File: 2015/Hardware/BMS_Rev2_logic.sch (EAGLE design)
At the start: 34 parts, among them Q9 MOSFET-NCHANNEL2N7002PW

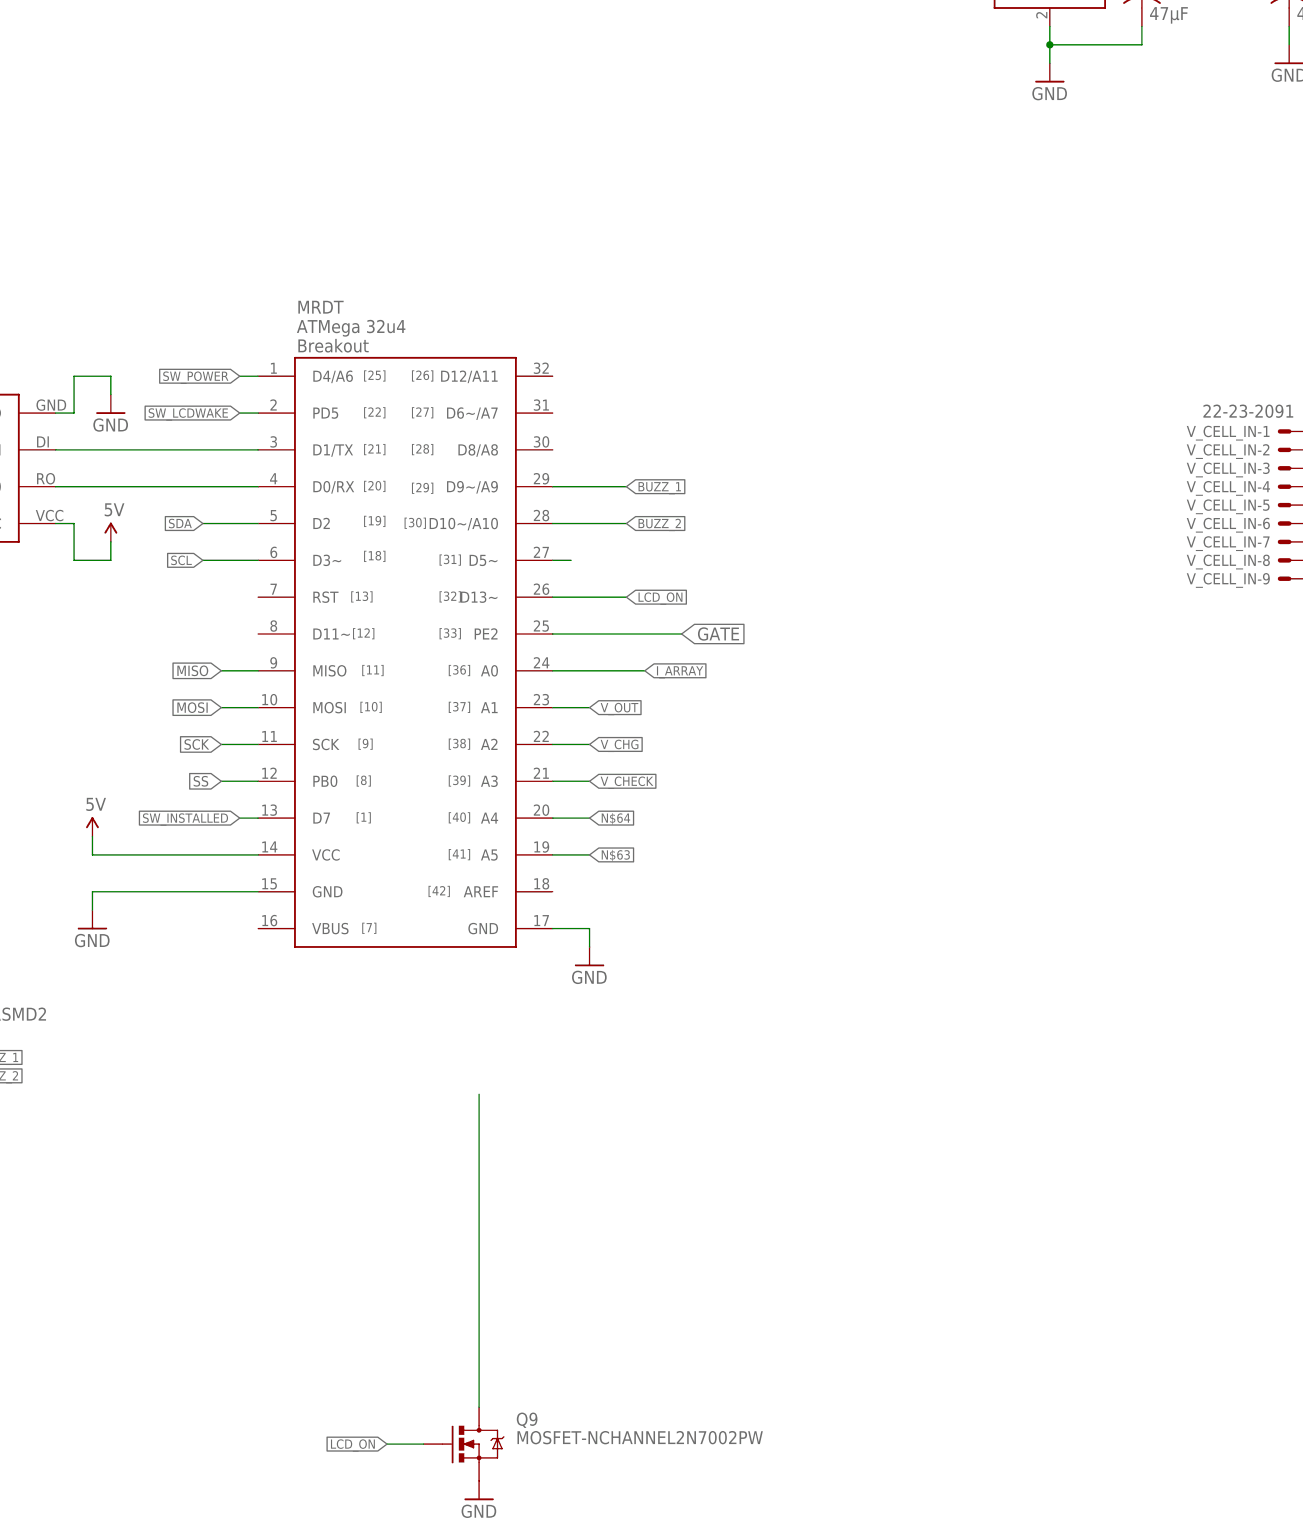
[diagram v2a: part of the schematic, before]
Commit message: Added connection for LCD
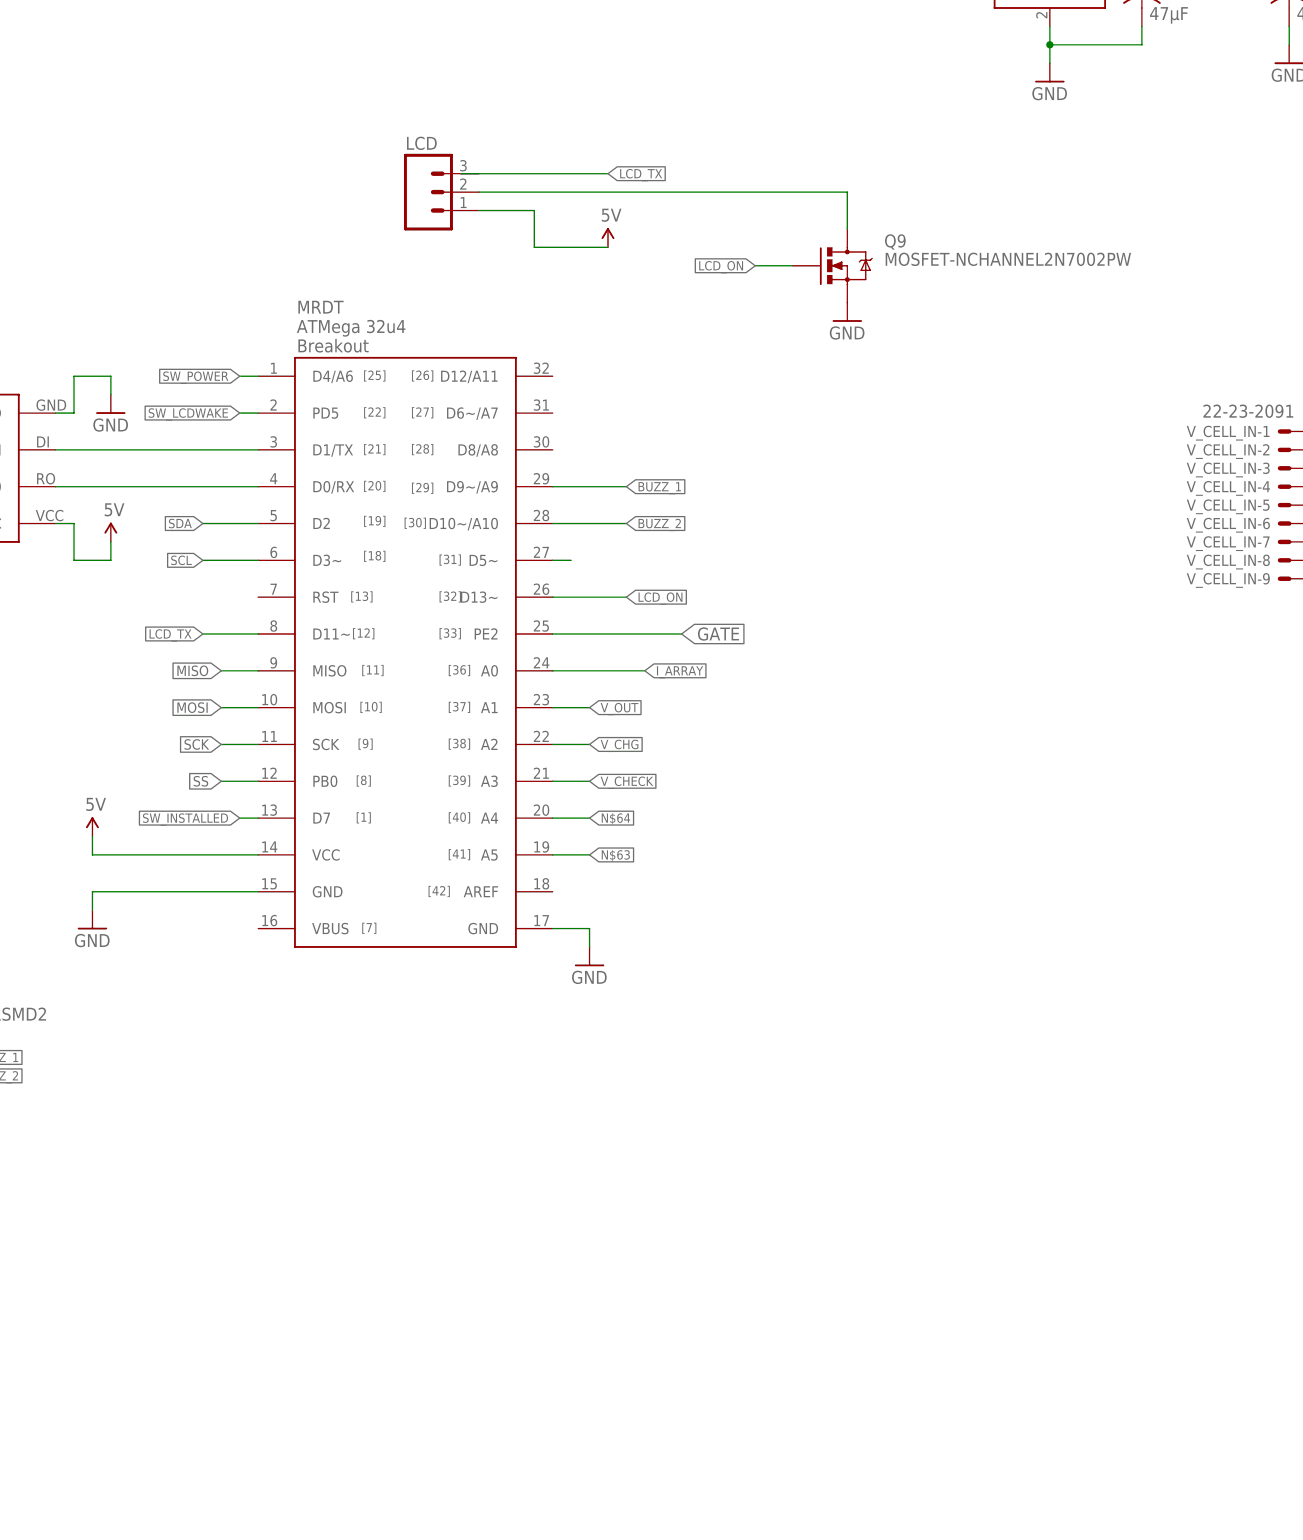
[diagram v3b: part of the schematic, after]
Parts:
- added LCD: (no value), SparkFun-Connectors:M03POLAR
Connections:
- removed net N$32: Q9.D
- new net LCD_TX: U$3.D11~
- new net N$5: LCD.2, Q9.D
- net 5V: now also LCD.1
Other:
- moved on the sheet: Q9
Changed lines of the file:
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@@
 <?xml version="1.0" encoding="utf-8"?>
 <!DOCTYPE eagle SYSTEM "eagle.dtd">
-<eagle version="7.0.0">
+<eagle version="6.5.0">
 <drawing>
 <settings>
@@
 <layers>
 <layer number="1" name="Top" color="4" fill="1" visible="no" active="no"/>
+<layer number="2" name="Route2" color="1" fill="3" visible="no" active="no"/>
+<layer number="3" name="Route3" color="4" fill="3" visible="no" active="no"/>
+<layer number="4" name="Route4" color="1" fill="4" visible="no" active="no"/>
+<layer number="5" name="Route5" color="4" fill="4" visible="no" active="no"/>
+<layer number="6" name="Route6" color="1" fill="8" visible="no" active="no"/>
+<layer number="7" name="Route7" color="4" fill="8" visible="no" active="no"/>
+<layer number="8" name="Route8" color="1" fill="2" visible="no" active="no"/>
+<layer number="9" name="Route9" color="4" fill="2" visible="no" active="no"/>
+<layer number="10" name="Route10" color="1" fill="7" visible="no" active="no"/>
+<layer number="11" name="Route11" color="4" fill="7" visible="no" active="no"/>
+<layer number="12" name="Route12" color="1" fill="5" visible="no" active="no"/>
+<layer number="13" name="Route13" color="4" fill="5" visible="no" active="no"/>
+<layer number="14" name="Route14" color="1" fill="6" visible="no" active="no"/>
+<layer number="15" name="Route15" color="4" fill="6" visible="no" active="no"/>
 <layer number="16" name="Bottom" color="1" fill="1" visible="no" active="no"/>
 <layer number="17" name="Pads" color="2" fill="1" visible="no" active="no"/>
@@
 <part name="GND2" library="SparkFun-Aesthetics" deviceset="GND" device=""/>
 <part name="F9" library="SparkFun-PowerIC" deviceset="PTC" device="SMD"/>
+<part name="LCD" library="SparkFun-Connectors" deviceset="M03" device="POLAR"/>
+<part name="SUPPLY3" library="SparkFun-Aesthetics" deviceset="5V" device=""/>
 </parts>
 <sheets>
@@
 <instance part="V_CELL_IN" gate="-8" x="88.9" y="-35.56" rot="R180"/>
 <instance part="V_CELL_IN" gate="-9" x="88.9" y="-38.1" rot="R180"/>
-<instance part="Q9" gate="G$1" x="-22.86" y="-157.48"/>
-<instance part="GND11" gate="1" x="-22.86" y="-165.1"/>
+<instance part="Q9" gate="G$1" x="27.94" y="5.08"/>
+<instance part="GND11" gate="1" x="27.94" y="-2.54"/>
 <instance part="JP3" gate="G$1" x="-129.54" y="60.96"/>
 <instance part="R7" gate="G$1" x="-111.76" y="60.96" rot="R270"/>
@@
 <instance part="GND2" gate="1" x="-27.94" y="83.82"/>
 <instance part="F9" gate="G$1" x="134.62" y="-58.42"/>
+<instance part="LCD" gate="G$1" x="-30.48" y="15.24"/>
+<instance part="SUPPLY3" gate="G$1" x="-5.08" y="7.62"/>
 </instances>
 <busses>
@@
 <wire x1="-15.24" y1="96.52" x2="-45.72" y2="96.52" width="0.1524" layer="91"/>
 <pinref part="SUPPLY2" gate="G$1" pin="5V"/>
+</segment>
+<segment>
+<pinref part="LCD" gate="G$1" pin="1"/>
+<wire x1="-22.86" y1="12.7" x2="-15.24" y2="12.7" width="0.1524" layer="91"/>
+<wire x1="-15.24" y1="12.7" x2="-15.24" y2="7.62" width="0.1524" layer="91"/>
+<pinref part="SUPPLY3" gate="G$1" pin="5V"/>
+<wire x1="-15.24" y1="7.62" x2="-5.08" y2="7.62" width="0.1524" layer="91"/>
 </segment>
 </net>
@@
 </segment>
 </net>
-<net name="N$32" class="0">
-<segment>
-<pinref part="Q9" gate="G$1" pin="D"/>
-<wire x1="-22.86" y1="-109.22" x2="-22.86" y2="-152.4" width="0.1524" layer="91"/>
-</segment>
-</net>
 <net name="LCD_ON" class="0">
 <segment>
 <pinref part="Q9" gate="G$1" pin="G"/>
-<wire x1="-30.48" y1="-157.48" x2="-35.56" y2="-157.48" width="0.1524" layer="91"/>
-<label x="-35.56" y="-157.48" size="1.27" layer="95" rot="R180" xref="yes"/>
+<wire x1="20.32" y1="5.08" x2="15.24" y2="5.08" width="0.1524" layer="91"/>
+<label x="15.24" y="5.08" size="1.27" layer="95" rot="R180" xref="yes"/>
 </segment>
 <segment>
@@
 </segment>
 </net>
+<net name="LCD_TX" class="0">
+<segment>
+<wire x1="-25.4" y1="17.78" x2="-5.08" y2="17.78" width="0.1524" layer="91"/>
+<label x="-5.08" y="17.78" size="1.27" layer="95" xref="yes"/>
+</segment>
+<segment>
+<pinref part="U$3" gate="G$1" pin="D11~"/>
+<wire x1="-53.34" y1="-45.72" x2="-60.96" y2="-45.72" width="0.1524" layer="91"/>
+<label x="-60.96" y="-45.72" size="1.27" layer="95" rot="R180" xref="yes"/>
+</segment>
+</net>
+<net name="N$5" class="0">
+<segment>
+<pinref part="LCD" gate="G$1" pin="2"/>
+<pinref part="Q9" gate="G$1" pin="D"/>
+<wire x1="-22.86" y1="15.24" x2="27.94" y2="15.24" width="0.1524" layer="91"/>
+<wire x1="27.94" y1="15.24" x2="27.94" y2="10.16" width="0.1524" layer="91"/>
+</segment>
+</net>
